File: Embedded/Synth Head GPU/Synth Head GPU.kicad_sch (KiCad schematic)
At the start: 28 parts, among them J1 10171746-00021LF, J2 JST [D], J3 JST [D], J4 JST [G], U10 FFC [G], U11 SRV05-4, U13 TCA9535RTWR, U5 FFC [D], U6 FFC [D], U7 FFC [C], U8 FFC [C], U9 FFC [U]

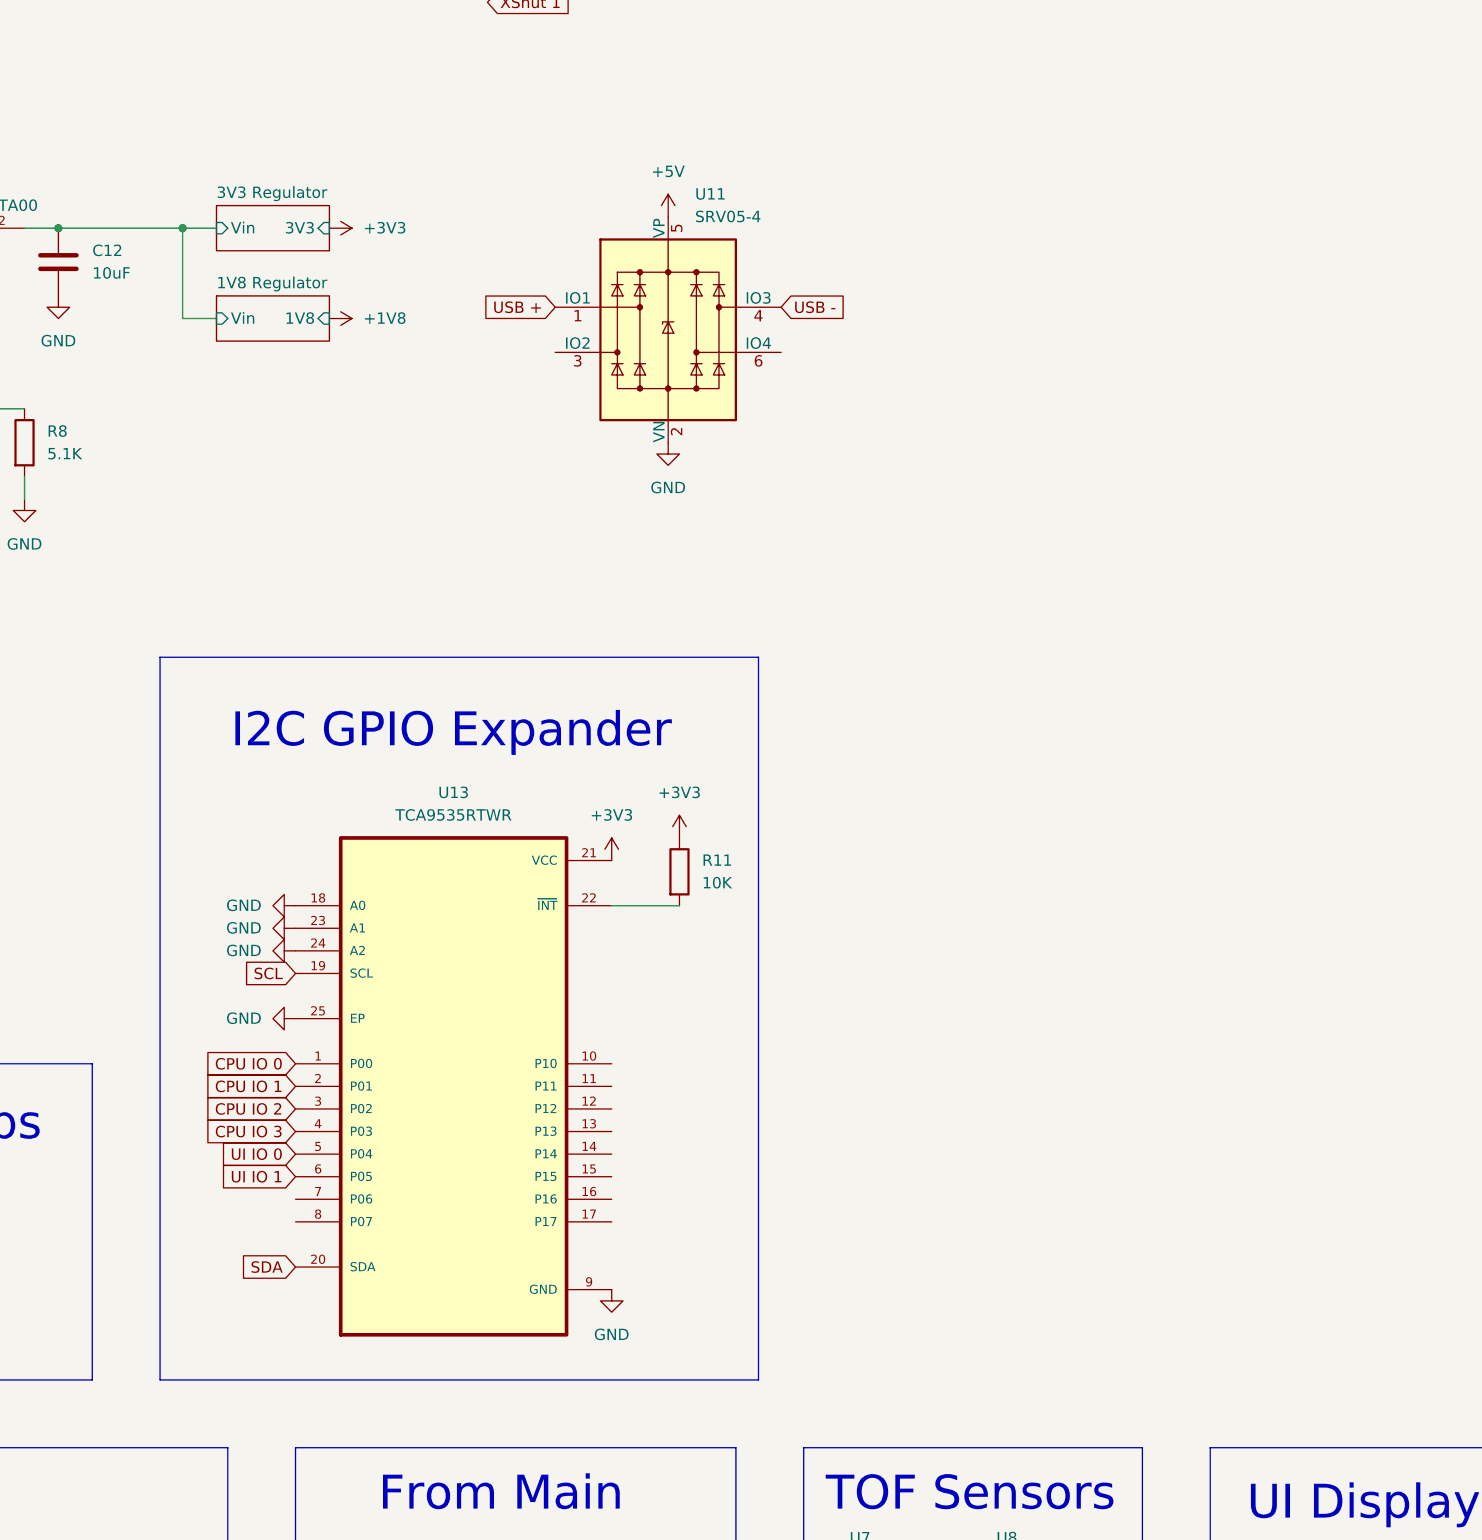
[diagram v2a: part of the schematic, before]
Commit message: Added Indicator Power LEDS & some Decoupling Caps
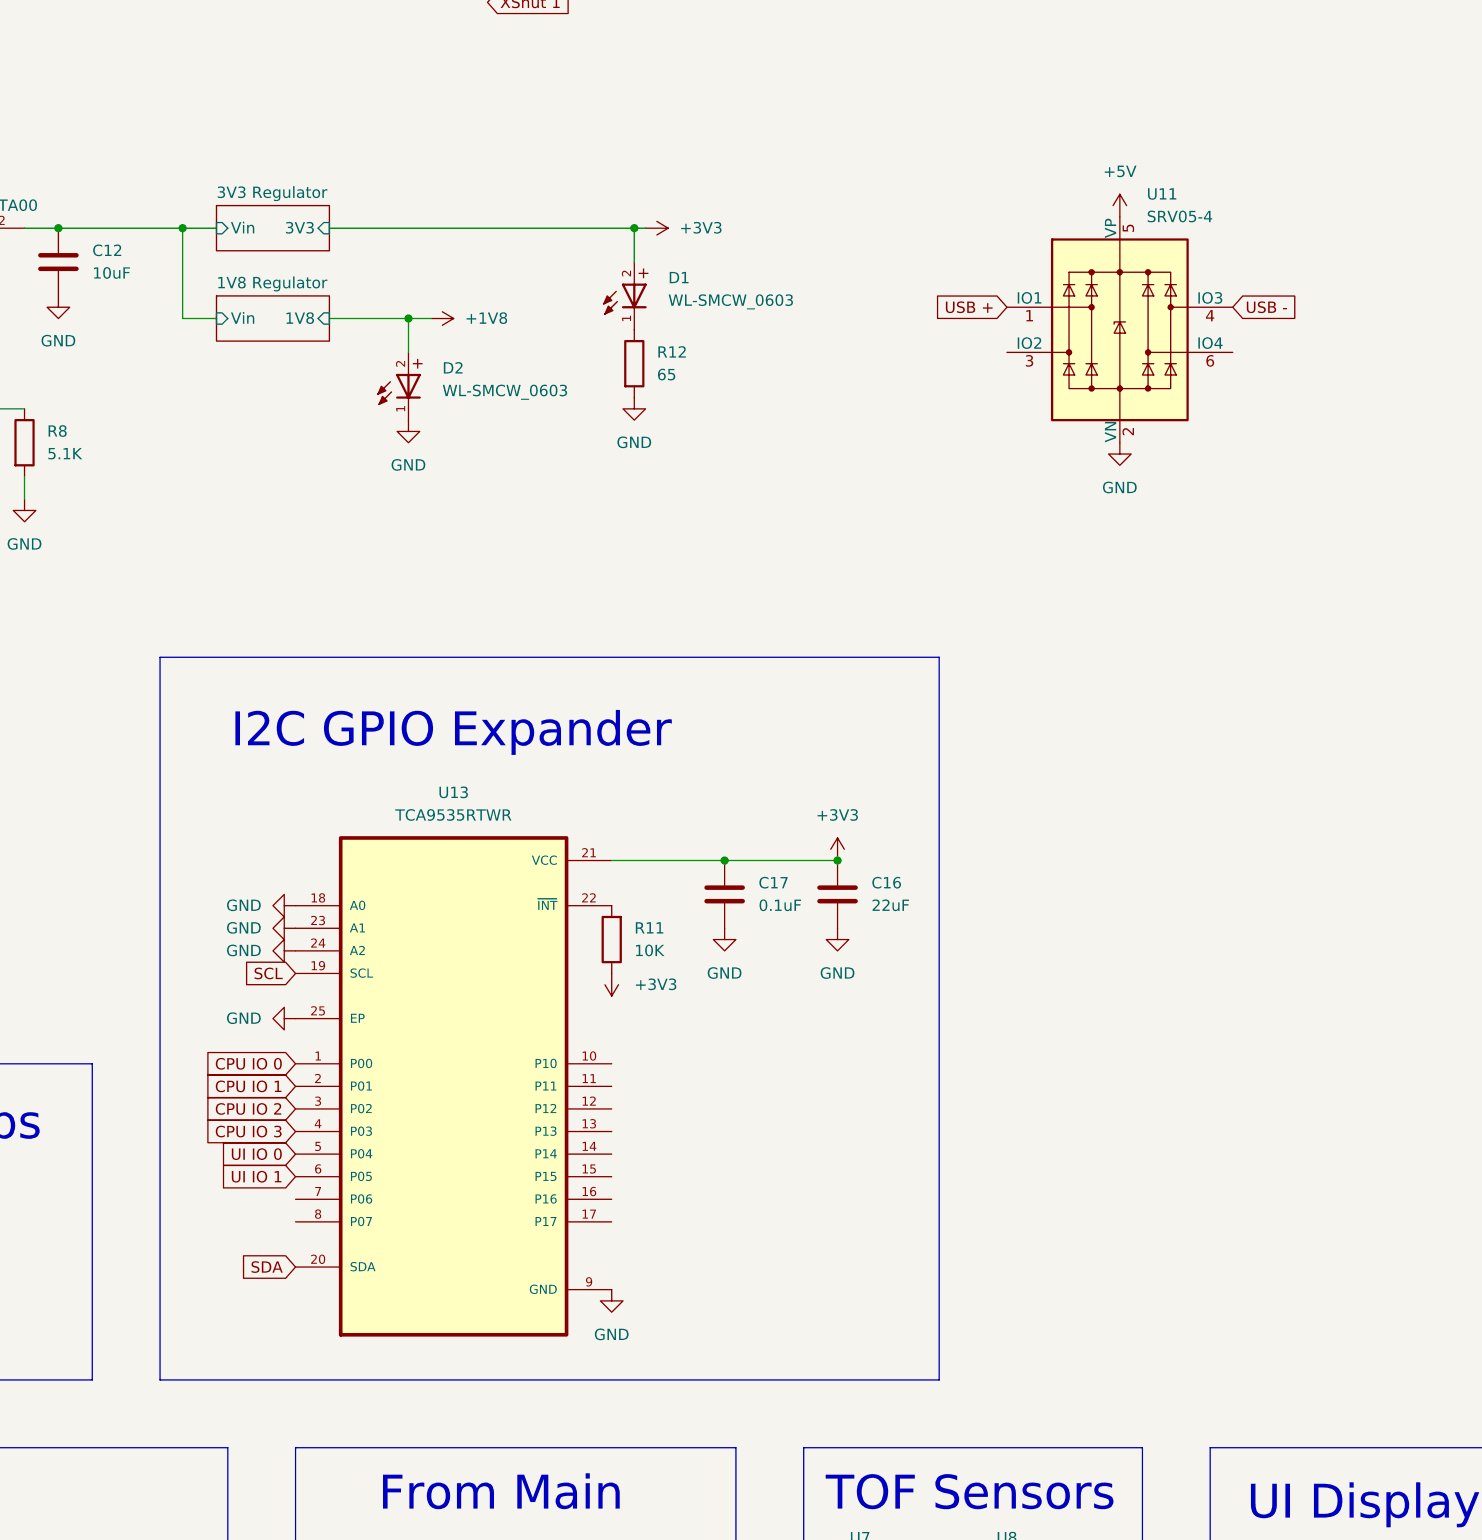
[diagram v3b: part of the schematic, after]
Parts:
- added C16: 22uF, Capacitor_SMD:C_0603_1608Metric_Pad1.08x0.95mm_HandSolder, symbol Device:C
- added C17: 0.1uF, Capacitor_SMD:C_0603_1608Metric, symbol Device:C
- added D1, D2: WL-SMCW_0603, LED_Red_SMD:WL-SMCW_0603, symbol LED_Red_SMD:WL-SMCW_0603
- added R12: 65, symbol Device:R
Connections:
- net +1V8: now also D2.2
- net +3V3: now also C16.1, C17.1, D1.2
- net GND: now also C16.2, C17.2, D2.1, R12.2
- new net: D1.1, R12.1
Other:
- moved on the sheet: R11, U11

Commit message: Prepared All Main Boards for PCB Creation
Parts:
- J2, J3: footprint (none) -> Connector_Molex:Molex_PicoBlade_53048-0410_1x04_P1.25mm_Horizontal
- J4: footprint (none) -> Connector_PinHeader_2.54mm:PinHeader_1x08_P2.54mm_Horizontal
- R12, R3, R4, R5: footprint (none) -> Resistor_SMD:R_0603_1608Metric_Pad0.98x0.95mm_HandSolder
- U10: footprint (none) -> FFC_Connector:FFC Aliexpress 0.5mm 12P
- U13: footprint TCA9535RTWR:QFN50P400X400X80-25N -> IO_Expander_TCA9535RTWR:QFN50P400X400X80-25N
- U7, U8: footprint (none) -> FFC_Connector:FFC Aliexpress 0.5mm 6P
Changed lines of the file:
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@@
 			)
 		)
-		(property "Footprint" ""
+		(property "Footprint" "FFC_Connector:FFC Aliexpress 0.5mm 6P"
 			(at 157.48 233.68 0)
 			(effects
@@
 			)
 		)
-		(property "Footprint" ""
+		(property "Footprint" "FFC_Connector:FFC Aliexpress 0.5mm 6P"
 			(at 173.99 233.68 0)
 			(effects
@@
 			)
 		)
-		(property "Footprint" ""
+		(property "Footprint" "Resistor_SMD:R_0603_1608Metric_Pad0.98x0.95mm_HandSolder"
 			(at 61.722 241.3 90)
 			(effects
@@
 			)
 		)
-		(property "Footprint" ""
+		(property "Footprint" "Connector_Molex:Molex_PicoBlade_53048-0410_1x04_P1.25mm_Horizontal"
 			(at 254 262.89 0)
 			(effects
@@
 			)
 		)
-		(property "Footprint" ""
+		(property "Footprint" "Connector_Molex:Molex_PicoBlade_53048-0410_1x04_P1.25mm_Horizontal"
 			(at 264.16 262.89 0)
 			(effects
@@
 			)
 		)
-		(property "Footprint" ""
+		(property "Footprint" "Connector_PinHeader_2.54mm:PinHeader_1x08_P2.54mm_Horizontal"
 			(at 109.22 234.95 0)
 			(effects
@@
 			)
 		)
-		(property "Footprint" ""
+		(property "Footprint" "Resistor_SMD:R_0603_1608Metric_Pad0.98x0.95mm_HandSolder"
 			(at 47.752 191.77 90)
 			(effects
@@
 			)
 		)
-		(property "Footprint" "TCA9535RTWR:QFN50P400X400X80-25N"
+		(property "Footprint" "IO_Expander_TCA9535RTWR:QFN50P400X400X80-25N"
 			(at 110.49 171.45 0)
 			(effects
@@
 			)
 		)
-		(property "Footprint" ""
+		(property "Footprint" "Resistor_SMD:R_0603_1608Metric_Pad0.98x0.95mm_HandSolder"
 			(at 31.242 191.77 90)
 			(effects
@@
 			)
 		)
-		(property "Footprint" ""
+		(property "Footprint" "Resistor_SMD:R_0603_1608Metric_Pad0.98x0.95mm_HandSolder"
 			(at 129.032 90.17 90)
 			(effects
@@
 			)
 		)
-		(property "Footprint" ""
+		(property "Footprint" "FFC_Connector:FFC Aliexpress 0.5mm 12P"
 			(at 124.46 236.22 0)
 			(effects

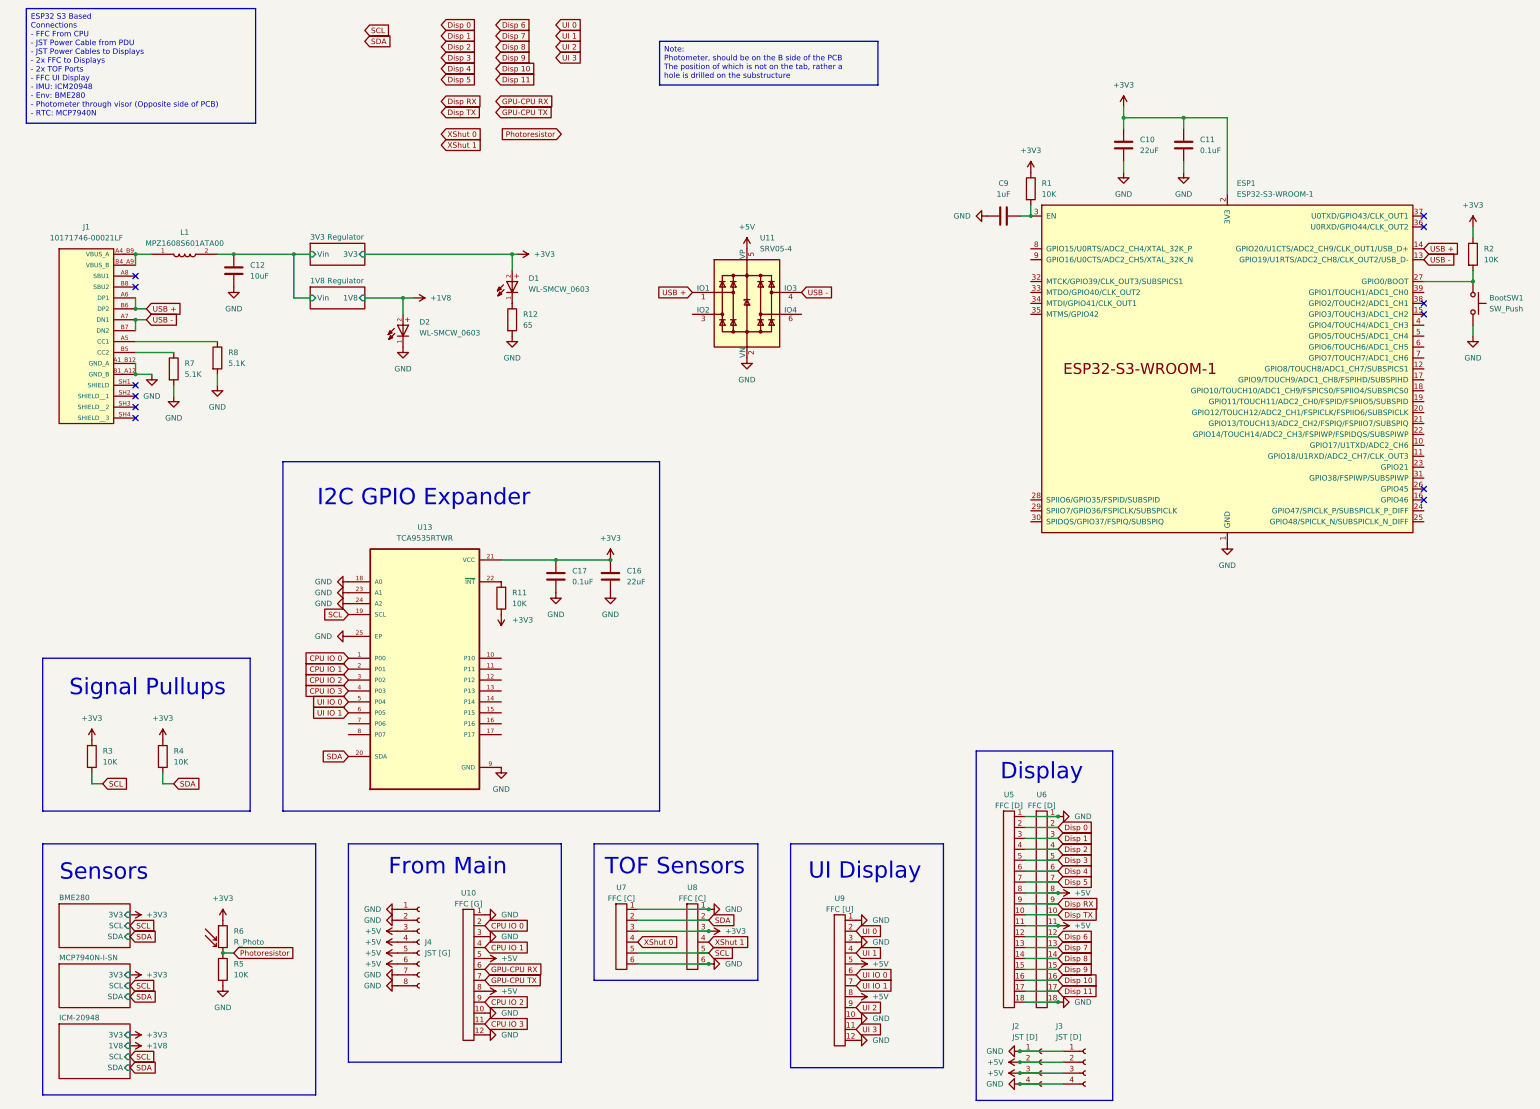
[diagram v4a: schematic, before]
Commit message: Added Misc Boards & Adapters
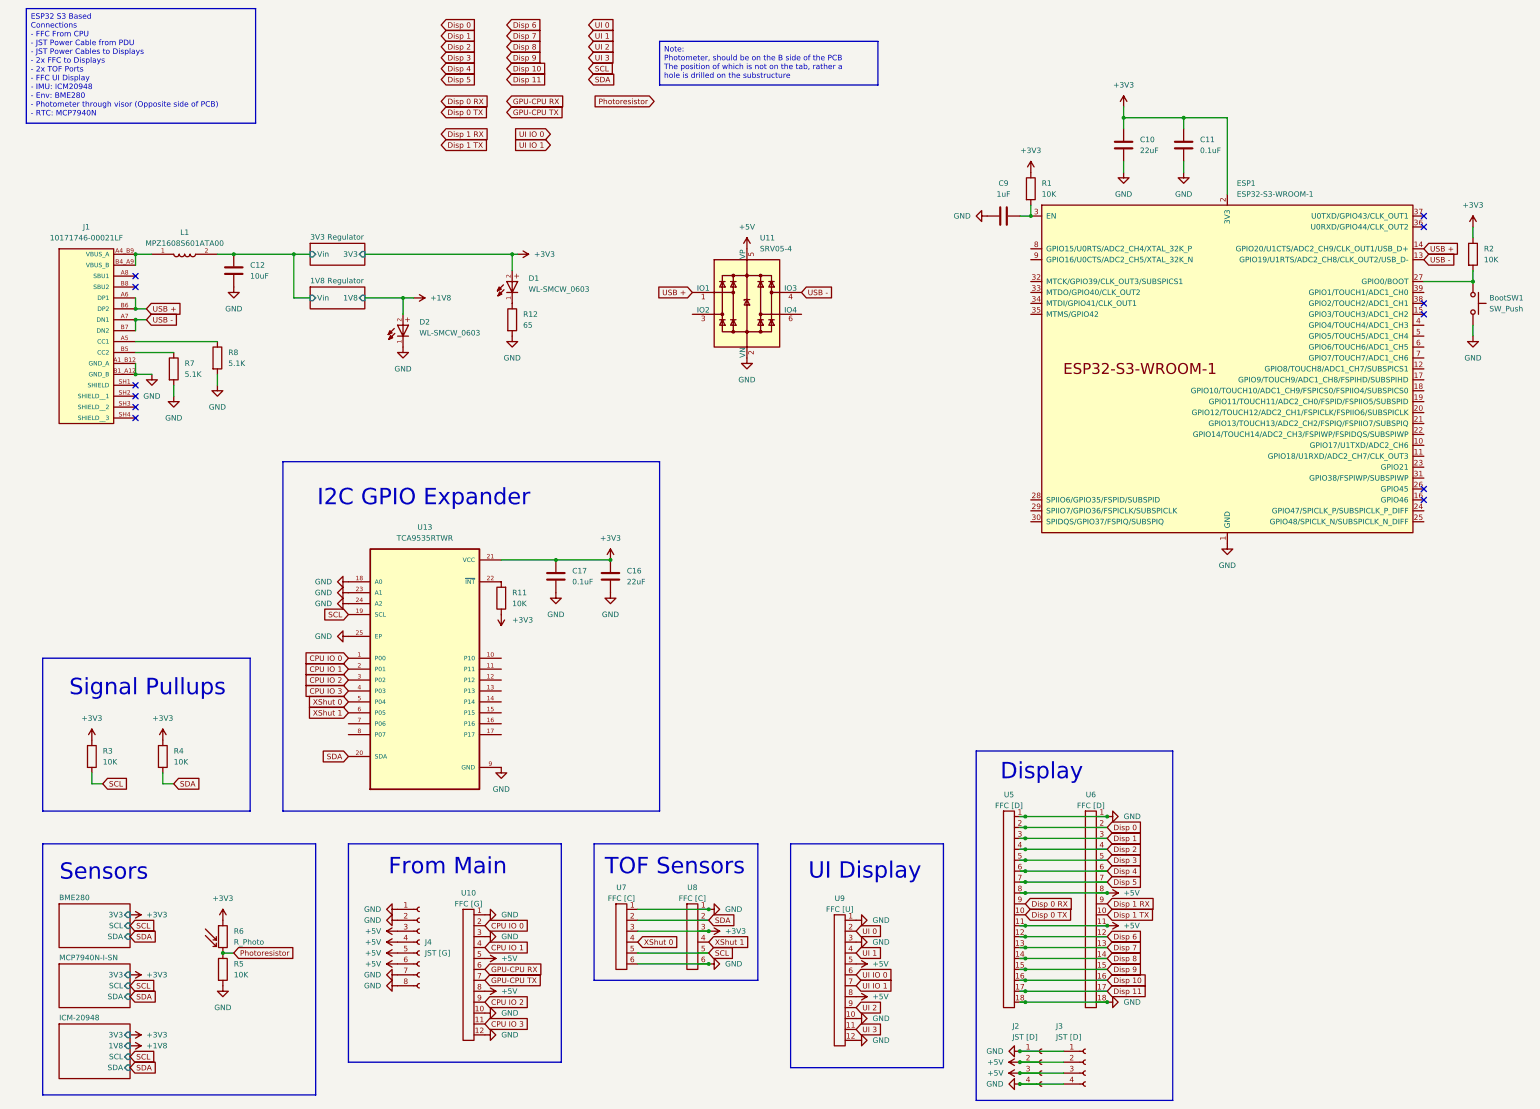
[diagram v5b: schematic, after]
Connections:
- net UI IO 0: no longer U13.5 (P04)
- net UI IO 1: no longer U13.6 (P05)
- net XShut 0: now also U13.5 (P04)
- net XShut 1: now also U13.6 (P05)
- net Disp RX renamed Disp 0 RX
- net Disp 0 RX: no longer U6.9
- net Disp TX renamed Disp 0 TX
- net Disp 0 TX: no longer U6.10
- new net Disp 1 RX: U6.9
- new net Disp 1 TX: U6.10
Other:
- moved on the sheet: U6

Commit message: Prepared Circuits for Routing and Placement Tuning
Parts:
- removed D2: WL-SMCW_0603, LED_Red_SMD:WL-SMCW_0603, symbol LED_Red_SMD:WL-SMCW_0603
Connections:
- net Disp 0: now also U5.17; no longer U5.2
- net Disp 1: now also U5.16; no longer U5.3
- net Disp 10: now also U5.3; no longer U5.16
- net Disp 11: now also U5.2; no longer U5.17
- net Disp 2: now also U5.15; no longer U5.4
- net Disp 3: now also U5.14; no longer U5.5
- net Disp 4: now also U5.13; no longer U5.6
- net Disp 5: now also U5.12; no longer U5.7
- net Disp 6: now also U5.7; no longer U5.12
- net Disp 7: now also U5.6; no longer U5.13
- net Disp 8: now also U5.5; no longer U5.14
- net Disp 9: now also U5.4; no longer U5.15
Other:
- moved on the sheet: D1, R12
